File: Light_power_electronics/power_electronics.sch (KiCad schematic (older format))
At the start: 1 part

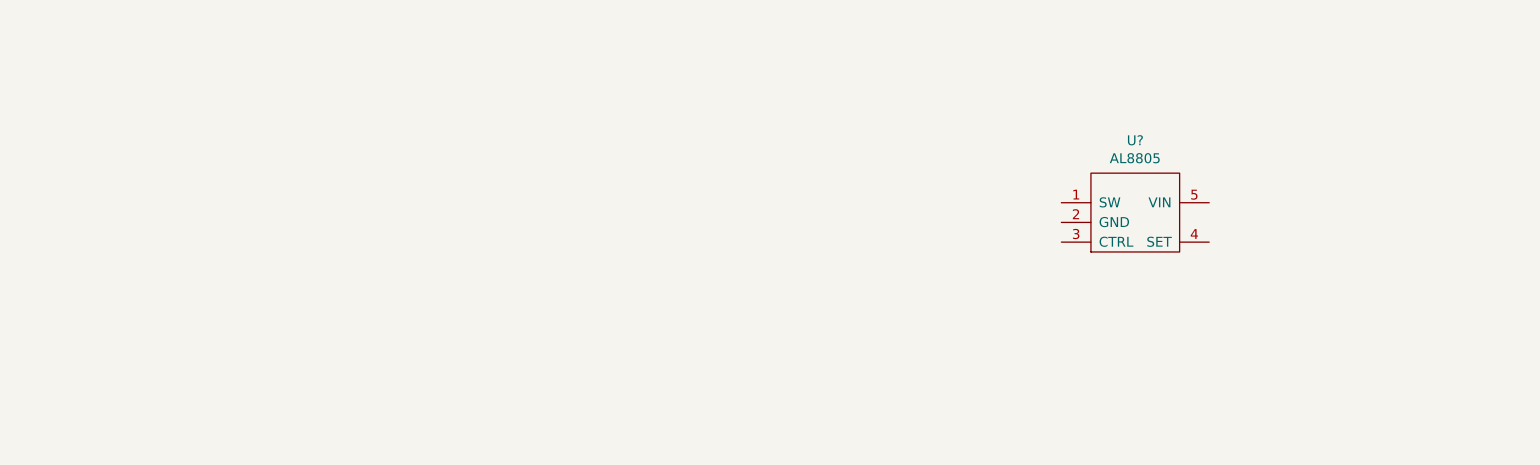
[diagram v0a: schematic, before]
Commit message: bulk of power electronics schematic done
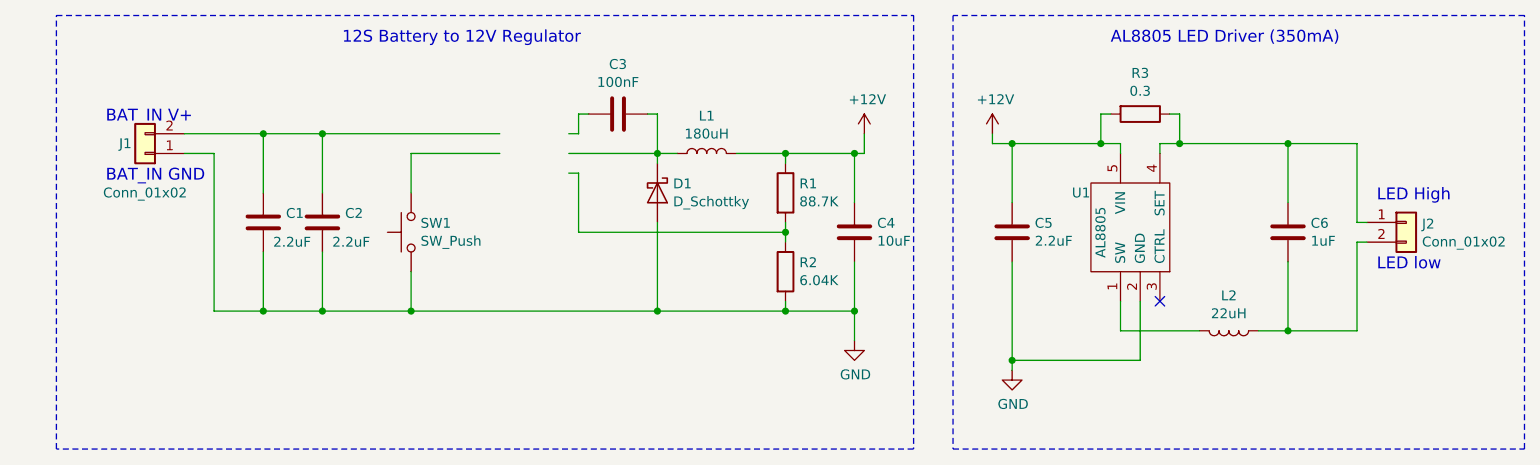
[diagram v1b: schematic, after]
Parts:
- added C1, C2, C5: 2.2uF, symbol C
- added C3: 100nF, symbol C
- added C4: 10uF, symbol C
- added C6: 1uF, symbol C
- added D1: D_Schottky, symbol D_Schottky
- added J1, J2: Conn_01x02, symbol Conn_01x02
- added L1: 180uH, symbol L
- added L2: 22uH, symbol L
- added R1: 88.7K, symbol R
- added R2: 6.04K, symbol R
- added R3: 0.3, symbol R
- added SW1: SW_Push, symbol SW_Push
- gave numbers to parts that had none: 1
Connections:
- net labels added: +12V, GND
- wire segments 0 -> 50
- no-connect marks 0 -> 1
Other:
- note added: "12S Battery to 12V Regulator"
- note added: "AL8805 LED Driver (350mA)"
- note added: "BAT_IN GND"
- note added: "BAT_IN V+"
- note added: "LED High"
- note added: "LED low"
- moved on the sheet: U1

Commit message: schematic done, adding footprints
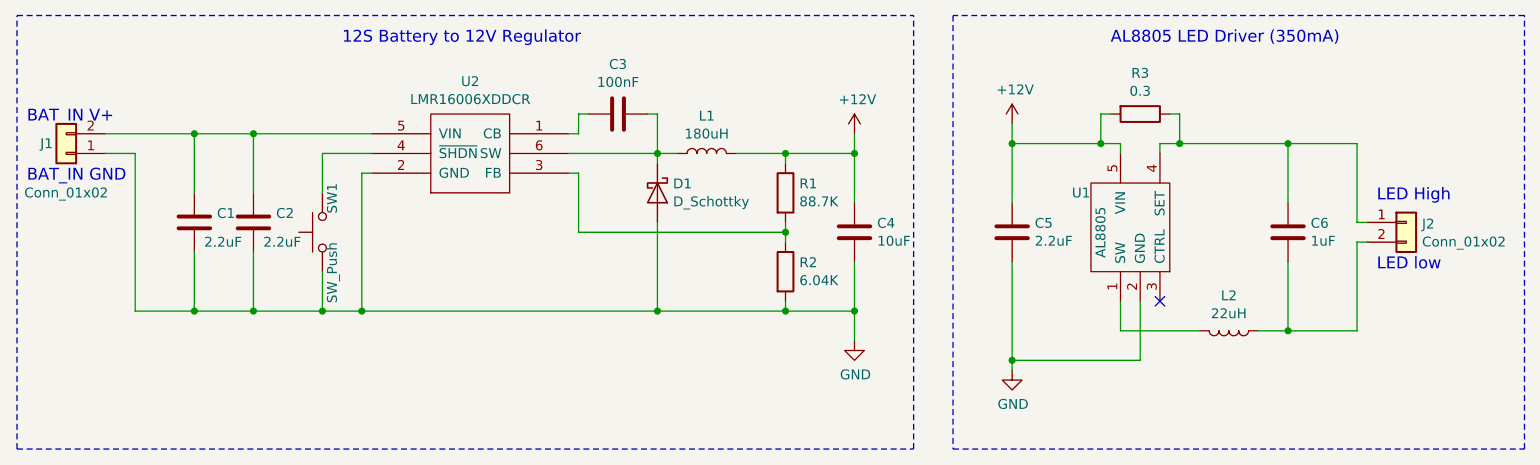
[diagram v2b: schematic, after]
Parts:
- added U2: LMR16006XDDCR, TO_SOT_Packages_SMD:SOT-23-6, symbol LMR16006XDDCR
- C1, C2: footprint (none) -> Capacitors_SMD:C_0805
- C3, C4, C5, C6: footprint (none) -> Capacitors_SMD:C_0603
- L2: footprint (none) -> Inductors_SMD:L_Taiyo-Yuden_NR-40xx
- R1, R2, R3: footprint (none) -> Resistors_SMD:R_0603
- U1: footprint MODULE -> TO_SOT_Packages_SMD:SOT-23-5
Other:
- moved on the sheet: C1, C2, J1, SW1
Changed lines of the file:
@@
 F 0 "U1" V 7100 3700 50  0000 C CNN
 F 1 "AL8805" H 6900 3600 50  0000 C CNN
-F 2 "MODULE" H 7000 3100 50  0001 C CNN
+F 2 "TO_SOT_Packages_SMD:SOT-23-5" H 7000 3100 50  0001 C CNN
 F 3 "DOCUMENTATION" H 6850 3200 50  0001 C CNN
 	1    6950 3400
@@
 F 0 "R3" V 6743 2850 50  0000 C CNN
 F 1 "0.3" V 6834 2850 50  0000 C CNN
-F 2 "" V 6880 2850 50  0001 C CNN
+F 2 "Resistors_SMD:R_0603" V 6880 2850 50  0001 C CNN
 F 3 "" H 6950 2850 50  0001 C CNN
 	1    6950 2850
@@
 	6800 2850 6750 2850
 Wire Wire Line
-	6750 2850 6750 3000
-Wire Wire Line
-	6200 3000 6850 3000
+	6750 3000 6750 2850
+Wire Wire Line
+	6300 3000 6850 3000
 Wire Wire Line
 	6850 3000 6850 3050
@@
 F 0 "C5" H 6415 3496 50  0000 L CNN
 F 1 "2.2uF" H 6415 3405 50  0000 L CNN
-F 2 "" H 6338 3300 50  0001 C CNN
+F 2 "Capacitors_SMD:C_0603" H 6338 3300 50  0001 C CNN
 F 3 "" H 6300 3450 50  0001 C CNN
 	1    6300 3450
@@
 F 0 "C6" H 7815 3496 50  0000 L CNN
 F 1 "1uF" H 7815 3405 50  0000 L CNN
-F 2 "" H 7738 3300 50  0001 C CNN
+F 2 "Capacitors_SMD:C_0603" H 7738 3300 50  0001 C CNN
 F 3 "" H 7700 3450 50  0001 C CNN
 	1    7700 3450
@@
 F 0 "L2" V 7222 3950 50  0000 C CNN
 F 1 "22uH" V 7313 3950 50  0000 C CNN
-F 2 "" H 7400 3950 50  0001 C CNN
+F 2 "Inductors_SMD:L_Taiyo-Yuden_NR-40xx" H 7400 3950 50  0001 C CNN
 F 3 "" H 7400 3950 50  0001 C CNN
 	1    7400 3950
@@
 NoConn ~ 7050 3800
 Wire Wire Line
-	6300 3000 6300 3300
+	6300 2900 6300 3300
 Connection ~ 6750 3000
-Wire Wire Line
-	6200 3000 6200 2950
 Connection ~ 6300 3000
 $Comp
 L +12V #PWR03
 U 1 1 5A66C7B7
-P 6200 2950
-F 0 "#PWR03" H 6200 2800 50  0001 C CNN
-F 1 "+12V" H 6215 3123 50  0000 C CNN
-F 2 "" H 6200 2950 50  0001 C CNN
-F 3 "" H 6200 2950 50  0001 C CNN
-	1    6200 2950
+P 6300 2900
+F 0 "#PWR03" H 6300 2750 50  0001 C CNN
+F 1 "+12V" H 6315 3073 50  0000 C CNN
+F 2 "" H 6300 2900 50  0001 C CNN
+F 3 "" H 6300 2900 50  0001 C CNN
+	1    6300 2900
 	1    0    0    -1
 $EndComp
@@
 L +12V #PWR02
 U 1 1 5A66C7F3
-P 5550 2950
-F 0 "#PWR02" H 5550 2800 50  0001 C CNN
-F 1 "+12V" H 5565 3123 50  0000 C CNN
-F 2 "" H 5550 2950 50  0001 C CNN
-F 3 "" H 5550 2950 50  0001 C CNN
-	1    5550 2950
+P 5500 2950
+F 0 "#PWR02" H 5500 2800 50  0001 C CNN
+F 1 "+12V" H 5515 3123 50  0000 C CNN
+F 2 "" H 5500 2950 50  0001 C CNN
+F 3 "" H 5500 2950 50  0001 C CNN
+	1    5500 2950
 	1    0    0    -1
 $EndComp
@@
 L Conn_01x02 J1
 U 1 1 5A66C932
-P 1900 3050
-F 0 "J1" H 2000 3000 50  0000 C CNN
-F 1 "Conn_01x02" H 1900 3250 50  0000 C CNN
-F 2 "" H 1900 3050 50  0001 C CNN
-F 3 "" H 1900 3050 50  0001 C CNN
-	1    1900 3050
+P 1500 3050
+F 0 "J1" H 1600 3000 50  0000 C CNN
+F 1 "Conn_01x02" H 1500 3250 50  0000 C CNN
+F 2 "" H 1500 3050 50  0001 C CNN
+F 3 "" H 1500 3050 50  0001 C CNN
+	1    1500 3050
 	-1   0    0    1
 $EndComp
@@
 F 0 "R1" H 5220 3296 50  0000 L CNN
 F 1 "88.7K" H 5220 3205 50  0000 L CNN
-F 2 "" V 5080 3250 50  0001 C CNN
+F 2 "Resistors_SMD:R_0603" V 5080 3250 50  0001 C CNN
 F 3 "" H 5150 3250 50  0001 C CNN
 	1    5150 3250
@@
 F 0 "R2" H 5220 3696 50  0000 L CNN
 F 1 "6.04K" H 5220 3605 50  0000 L CNN
-F 2 "" V 5080 3650 50  0001 C CNN
+F 2 "Resistors_SMD:R_0603" V 5080 3650 50  0001 C CNN
 F 3 "" H 5150 3650 50  0001 C CNN
 	1    5150 3650
@@
 F 0 "C4" H 5615 3496 50  0000 L CNN
 F 1 "10uF" H 5615 3405 50  0000 L CNN
-F 2 "" H 5538 3300 50  0001 C CNN
+F 2 "Capacitors_SMD:C_0603" H 5538 3300 50  0001 C CNN
 F 3 "" H 5500 3450 50  0001 C CNN
 	1    5500 3450
@@
 F 0 "C3" V 4048 2850 50  0000 C CNN
 F 1 "100nF" V 4139 2850 50  0000 C CNN
-F 2 "" H 4338 2700 50  0001 C CNN
+F 2 "Capacitors_SMD:C_0603" H 4338 2700 50  0001 C CNN
 F 3 "" H 4300 2850 50  0001 C CNN
 	1    4300 2850
@@
 L C C2
 U 1 1 5A66CDB6
-P 2800 3400
-F 0 "C2" H 2915 3446 50  0000 L CNN
-F 1 "2.2uF" H 2850 3300 50  0000 L CNN
-F 2 "" H 2838 3250 50  0001 C CNN
-F 3 "" H 2800 3400 50  0001 C CNN
-	1    2800 3400
+P 2450 3400
+F 0 "C2" H 2565 3446 50  0000 L CNN
+F 1 "2.2uF" H 2500 3300 50  0000 L CNN
+F 2 "Capacitors_SMD:C_0805" H 2488 3250 50  0001 C CNN
+F 3 "" H 2450 3400 50  0001 C CNN
+	1    2450 3400
 	1    0    0    -1
 $EndComp
@@
 L C C1
 U 1 1 5A66CDFC
-P 2500 3400
-F 0 "C1" H 2615 3446 50  0000 L CNN
-F 1 "2.2uF" H 2550 3300 50  0000 L CNN
-F 2 "" H 2538 3250 50  0001 C CNN
-F 3 "" H 2500 3400 50  0001 C CNN
-	1    2500 3400
+P 2150 3400
+F 0 "C1" H 2265 3446 50  0000 L CNN
+F 1 "2.2uF" H 2200 3300 50  0000 L CNN
+F 2 "Capacitors_SMD:C_0805" H 2188 3250 50  0001 C CNN
+F 3 "" H 2150 3400 50  0001 C CNN
+	1    2150 3400
 	1    0    0    -1
 $EndComp
@@
 	5150 3100 5150 3050
 Wire Wire Line
-	4900 3050 5550 3050
-Wire Wire Line
-	5500 3050 5500 3300
+	4900 3050 5500 3050
+Wire Wire Line
+	5500 2950 5500 3300
 Connection ~ 5150 3050
-Wire Wire Line
-	5550 3050 5550 2950
 Connection ~ 5500 3050
 $Comp
@@
 	5150 3850 5150 3800
 Wire Wire Line
-	2250 3850 5500 3850
+	1850 3850 5500 3850
 Connection ~ 5500 3850
 Wire Wire Line
@@
 Connection ~ 5150 3850
 Wire Wire Line
-	2500 3550 2500 3850
+	2150 3550 2150 3850
 Connection ~ 4500 3850
 Wire Wire Line
-	2800 3550 2800 3850
-Connection ~ 2800 3850
+	2450 3550 2450 3850
+Connection ~ 2450 3850
 Wire Wire Line
 	4500 2850 4500 3100
@@
 Connection ~ 4500 3050
 Wire Wire Line
-	2100 3050 2250 3050
-Wire Wire Line
-	2250 3050 2250 3850
-Connection ~ 2500 3850
-Text Notes 1700 3200 0    60   ~ 0
+	1700 3050 1850 3050
+Wire Wire Line
+	1850 3050 1850 3850
+Connection ~ 2150 3850
+Text Notes 1300 3200 0    60   ~ 0
 BAT_IN GND
-Text Notes 1700 2900 0    60   ~ 0
+Text Notes 1300 2900 0    60   ~ 0
 BAT_IN V+
 Wire Wire Line
@@
 Connection ~ 5150 3450
 Wire Wire Line
-	2100 2950 3700 2950
-Wire Wire Line
-	2500 2950 2500 3250
-Connection ~ 2500 2950
-Wire Wire Line
-	2800 3250 2800 2950
-Connection ~ 2800 2950
+	1700 2950 3050 2950
+Wire Wire Line
+	2150 2950 2150 3250
+Connection ~ 2150 2950
+Wire Wire Line
+	2450 3250 2450 2950
+Connection ~ 2450 2950
 $Comp
 L SW_Push SW1
 U 1 1 5A66DDFE
-P 3250 3450
-F 0 "SW1" V 3296 3402 50  0000 R CNN
-F 1 "SW_Push" V 3205 3402 50  0000 R CNN
-F 2 "" H 3250 3650 50  0001 C CNN
-F 3 "" H 3250 3650 50  0001 C CNN
-	1    3250 3450
+P 2800 3450
+F 0 "SW1" H 3050 3400 50  0000 R CNN
+F 1 "SW_Push" H 2750 3400 50  0000 R CNN
+F 2 "" H 2800 3650 50  0001 C CNN
+F 3 "" H 2800 3650 50  0001 C CNN
+	1    2800 3450
 	0    -1   -1   0
 $EndComp
 Wire Wire Line
-	3250 3250 3250 3050
-Wire Wire Line
-	3250 3050 3700 3050
-Wire Wire Line
-	3250 3650 3250 3850
-Connection ~ 3250 3850
-Wire Notes Line
-	5800 2350 5800 4550
-Wire Notes Line
-	5800 4550 1450 4550
-Wire Notes Line
-	1450 4550 1450 2350
-Wire Notes Line
-	1450 2350 5800 2350
+	2800 3250 2800 3050
+Wire Wire Line
+	2800 3050 3050 3050
+Wire Wire Line
+	2800 3650 2800 3850
+Connection ~ 2800 3850
+Wire Notes Line
+	5800 4550 5800 2350
+Wire Notes Line
+	1250 4550 5800 4550
+Wire Notes Line
+	1250 4550 1250 2350
+Wire Notes Line
+	1250 2350 5800 2350
 Wire Notes Line
 	6000 2350 6000 4550
@@
 Text Notes 2900 2500 0    60   ~ 0
 12S Battery to 12V Regulator
+$Comp
+L LMR16006XDDCR U2
+U 1 1 5A67FDCF
+P 3550 3050
+F 0 "U2" H 3550 3415 50  0000 C CNN
+F 1 "LMR16006XDDCR" H 3550 3324 50  0000 C CNN
+F 2 "TO_SOT_Packages_SMD:SOT-23-6" H 3750 2700 50  0001 C CNN
+F 3 "DOCUMENTATION" H 3600 2800 50  0001 C CNN
+	1    3550 3050
+	1    0    0    -1
+$EndComp
+Wire Wire Line
+	3050 3150 3000 3150
+Wire Wire Line
+	3000 3150 3000 3850
+Connection ~ 3000 3850
 $EndSCHEMATC
